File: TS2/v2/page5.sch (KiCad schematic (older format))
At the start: 4 parts, among them U15 HM6264, U16 2764, U17 HM6264, U18 2764

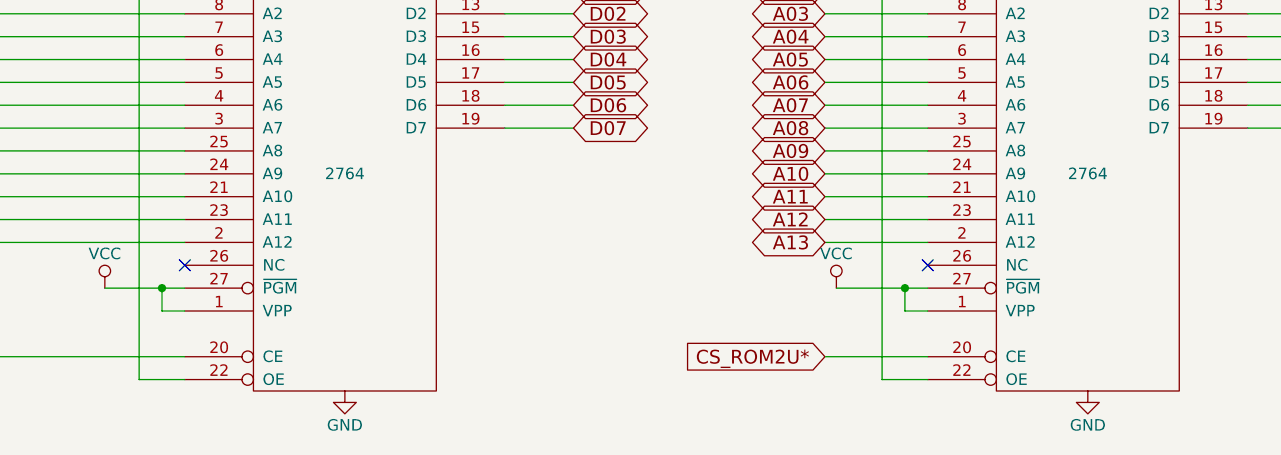
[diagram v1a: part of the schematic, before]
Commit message: Use 28C64 EEPROM instead of 27C64 EPROM.
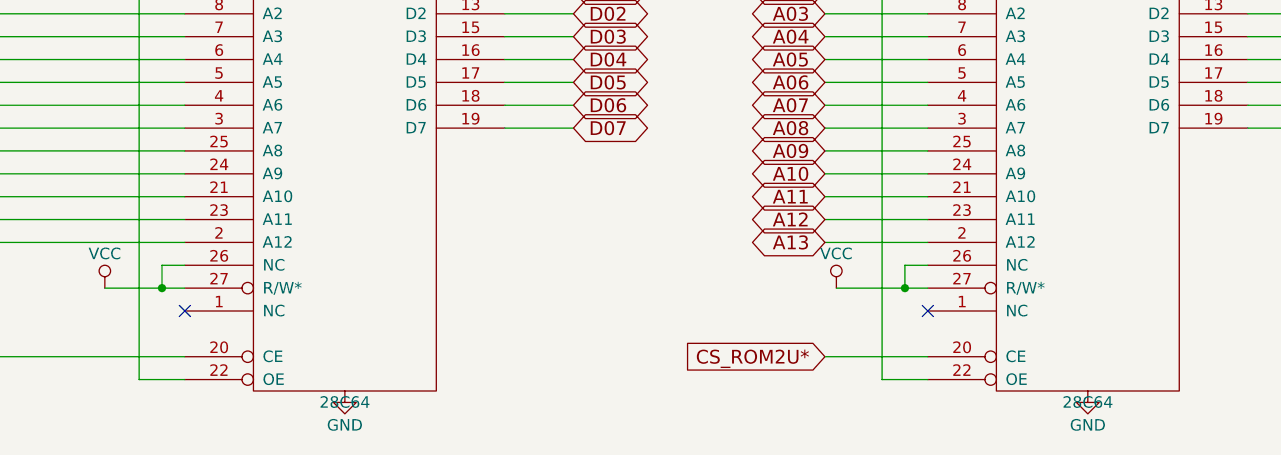
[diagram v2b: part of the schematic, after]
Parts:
- removed U16, U18: 2764, symbol 2764
- added U16, U18: 28C64, symbol 28C64
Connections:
- net A01: now also U16.10 (A0), U18.10 (A0)
- net A02: now also U16.9 (A1), U18.9 (A1)
- net A03: now also U16.8 (A2), U18.8 (A2)
- net A04: now also U16.7 (A3), U18.7 (A3)
- net A05: now also U16.6 (A4), U18.6 (A4)
- net A06: now also U16.5 (A5), U18.5 (A5)
- net A07: now also U16.4 (A6), U18.4 (A6)
- net A08: now also U16.3 (A7), U18.3 (A7)
- net A09: now also U16.25 (A8), U18.25 (A8)
- net A10: now also U16.24 (A9), U18.24 (A9)
- net A11: now also U16.21 (A10), U18.21 (A10)
- net A12: now also U16.23 (A11), U18.23 (A11)
- net A13: now also U16.2 (A12), U18.2 (A12)
- net CS_ROM2L*: now also U16.20 (CE)
- net CS_ROM2U*: now also U18.20 (CE)
- net D00: now also U16.11 (D0)
- net D01: now also U16.12 (D1)
- net D02: now also U16.13 (D2)
- net D03: now also U16.15 (D3)
- net D04: now also U16.16 (D4)
- net D05: now also U16.17 (D5)
- net D06: now also U16.18 (D6)
- net D07: now also U16.19 (D7)
- net D08: now also U18.11 (D0)
- net D09: now also U18.12 (D1)
- net D10: now also U18.13 (D2)
- net D11: now also U18.15 (D3)
- net D12: now also U18.16 (D4)
- net D13: now also U18.17 (D5)
- net D14: now also U18.18 (D6)
- net D15: now also U18.19 (D7)
- net GND: now also U16.14 (GND), U18.14 (GND)
- net R*/W: now also U16.22 (OE), U18.22 (OE)
- net VCC: now also U16.26 (NC), U16.27 (R/W*), U16.28 (VCC), U18.26 (NC), U18.27 (R/W*), U18.28 (VCC)
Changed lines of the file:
@@
 $EndDescr
-$Comp
-L 2764 U16
-U 1 1 57CAE145
-P 4350 5100
-F 0 "U16" H 4100 6100 50  0000 C CNN
-F 1 "2764" H 4350 5100 50  0000 C CNN
-F 2 "" H 4350 5100 50  0000 C CNN
-F 3 "" H 4350 5100 50  0000 C CNN
-	1    4350 5100
-	1    0    0    -1
-$EndComp
-$Comp
-L 2764 U18
-U 1 1 57CAE146
-P 7600 5100
-F 0 "U18" H 7350 6100 50  0000 C CNN
-F 1 "2764" H 7600 5100 50  0000 C CNN
-F 2 "" H 7600 5100 50  0000 C CNN
-F 3 "" H 7600 5100 50  0000 C CNN
-	1    7600 5100
-	1    0    0    -1
-$EndComp
 $Comp
 L HM6264 U15
@@
 Wire Wire Line
 	3300 5600 3650 5600
-Wire Wire Line
-	3650 5700 3550 5700
-Wire Wire Line
-	3550 5700 3550 5600
 $Comp
 L VCC #PWR051
@@
 Wire Wire Line
 	2300 5900 3650 5900
-NoConn ~ 3650 5500
 Wire Wire Line
 	3650 5400 2300 5400
@@
 	1    0    0    -1
 $EndComp
-NoConn ~ 6900 5500
 Text GLabel 6450 4300 0    60   BiDi ~ 0
 A02
@@
 Wire Wire Line
 	6500 5600 6900 5600
-Wire Wire Line
-	6800 5600 6800 5700
-Wire Wire Line
-	6800 5700 6900 5700
 Connection ~ 6800 5600
 $Comp
@@
 Text GLabel 2300 3950 0    60   Input ~ 0
 R*/W
+$Comp
+L 28C64 U16
+U 1 1 57D4FDC8
+P 4350 5100
+F 0 "U16" H 4100 6100 50  0000 C CNN
+F 1 "28C64" H 4350 4100 50  0000 C CNN
+F 2 "" H 4350 5100 50  0000 C CNN
+F 3 "" H 4350 5100 50  0000 C CNN
+	1    4350 5100
+	1    0    0    -1
+$EndComp
+$Comp
+L 28C64 U18
+U 1 1 57D4FDF1
+P 7600 5100
+F 0 "U18" H 7350 6100 50  0000 C CNN
+F 1 "28C64" H 7600 4100 50  0000 C CNN
+F 2 "" H 7600 5100 50  0000 C CNN
+F 3 "" H 7600 5100 50  0000 C CNN
+	1    7600 5100
+	1    0    0    -1
+$EndComp
+Wire Wire Line
+	3550 5500 3650 5500
+Wire Wire Line
+	3550 5500 3550 5600
+NoConn ~ 3650 5700
+Wire Wire Line
+	6900 5500 6800 5500
+Wire Wire Line
+	6800 5500 6800 5600
+NoConn ~ 6900 5700
 $EndSCHEMATC

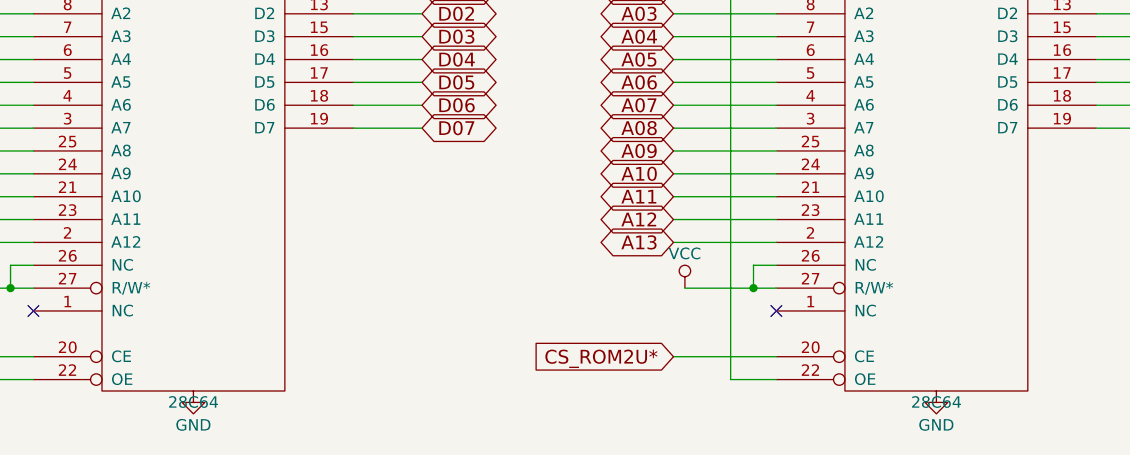
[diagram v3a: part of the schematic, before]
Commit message: Remove two duplicated pullup resistors. Route some signals better.
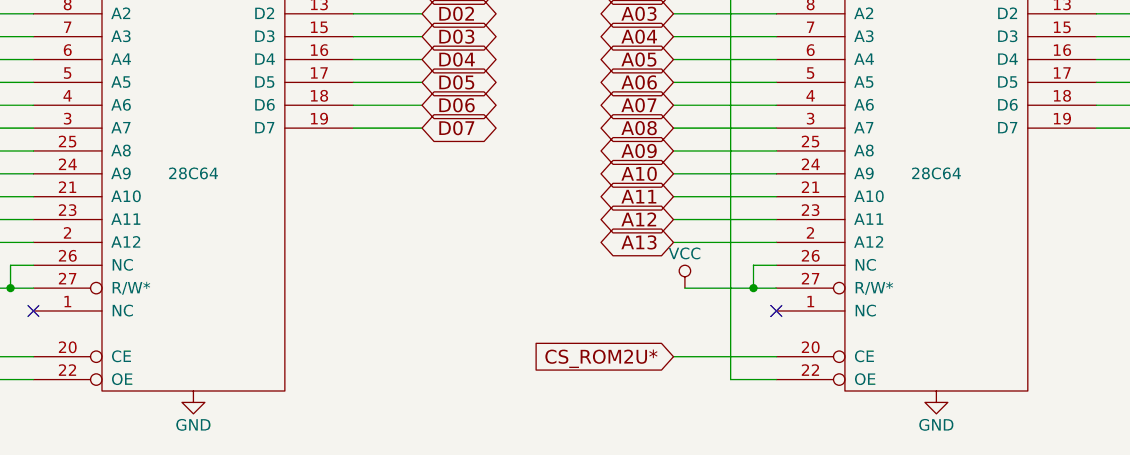
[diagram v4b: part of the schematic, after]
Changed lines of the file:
@@
 Sheet 6 8
 Title "TS2 68000 Single Board Computer"
-Date "2016-09-03"
+Date "2016-11-27"
 Rev "2.0"
 Comp "Jeff Tranter"
@@
 	5050 1650 5350 1650
 $Comp
-L GND #PWR045
+L GND #PWR044
 U 1 1 57C4A627
 P 5050 3250
-F 0 "#PWR045" H 5050 3000 50  0001 C CNN
+F 0 "#PWR044" H 5050 3000 50  0001 C CNN
 F 1 "GND" H 5050 3100 50  0000 C CNN
 F 2 "" H 5050 3250 50  0000 C CNN
@@
 $EndComp
 $Comp
-L VCC #PWR046
+L VCC #PWR045
 U 1 1 57C4A645
 P 5050 3150
-F 0 "#PWR046" H 5050 3000 50  0001 C CNN
+F 0 "#PWR045" H 5050 3000 50  0001 C CNN
 F 1 "VCC" H 5050 3300 50  0000 C CNN
 F 2 "" H 5050 3150 50  0000 C CNN
@@
 $EndComp
 $Comp
-L VCC #PWR047
+L VCC #PWR046
 U 1 1 57C4A66D
 P 8300 3150
-F 0 "#PWR047" H 8300 3000 50  0001 C CNN
+F 0 "#PWR046" H 8300 3000 50  0001 C CNN
 F 1 "VCC" H 8300 3300 50  0000 C CNN
 F 2 "" H 8300 3150 50  0000 C CNN
@@
 $EndComp
 $Comp
-L GND #PWR048
+L GND #PWR047
 U 1 1 57C4A68B
 P 8300 3250
-F 0 "#PWR048" H 8300 3000 50  0001 C CNN
+F 0 "#PWR047" H 8300 3000 50  0001 C CNN
 F 1 "GND" H 8300 3100 50  0000 C CNN
 F 2 "" H 8300 3250 50  0000 C CNN
@@
 A01
 $Comp
-L VCC #PWR049
+L VCC #PWR048
 U 1 1 57C4B0B4
 P 4350 1500
-F 0 "#PWR049" H 4350 1350 50  0001 C CNN
+F 0 "#PWR048" H 4350 1350 50  0001 C CNN
 F 1 "VCC" H 4350 1650 50  0000 C CNN
 F 2 "" H 4350 1500 50  0000 C CNN
@@
 $EndComp
 $Comp
-L GND #PWR050
+L GND #PWR049
 U 1 1 57C4B0FA
 P 4350 3400
-F 0 "#PWR050" H 4350 3150 50  0001 C CNN
+F 0 "#PWR049" H 4350 3150 50  0001 C CNN
 F 1 "GND" H 4350 3250 50  0000 C CNN
 F 2 "" H 4350 3400 50  0000 C CNN
@@
 CS_ROM2L*
 $Comp
-L GND #PWR051
+L GND #PWR050
 U 1 1 57C52013
 P 4350 6050
-F 0 "#PWR051" H 4350 5800 50  0001 C CNN
+F 0 "#PWR050" H 4350 5800 50  0001 C CNN
 F 1 "GND" H 4350 5900 50  0000 C CNN
 F 2 "" H 4350 6050 50  0000 C CNN
@@
 $EndComp
 $Comp
-L VCC #PWR052
+L VCC #PWR051
 U 1 1 57CAE14E
 P 4350 4150
-F 0 "#PWR052" H 4350 4000 50  0001 C CNN
+F 0 "#PWR051" H 4350 4000 50  0001 C CNN
 F 1 "VCC" H 4350 4300 50  0000 C CNN
 F 2 "" H 4350 4150 50  0000 C CNN
@@
 	3300 5600 3650 5600
 $Comp
-L VCC #PWR053
+L VCC #PWR052
 U 1 1 57CAE14F
 P 3300 5600
-F 0 "#PWR053" H 3300 5450 50  0001 C CNN
+F 0 "#PWR052" H 3300 5450 50  0001 C CNN
 F 1 "VCC" H 3300 5750 50  0000 C CNN
 F 2 "" H 3300 5600 50  0000 C CNN
@@
 Connection ~ 3650 3650
 $Comp
-L VCC #PWR054
+L VCC #PWR053
 U 1 1 57CAE150
 P 7600 1500
-F 0 "#PWR054" H 7600 1350 50  0001 C CNN
+F 0 "#PWR053" H 7600 1350 50  0001 C CNN
 F 1 "VCC" H 7600 1650 50  0000 C CNN
 F 2 "" H 7600 1500 50  0000 C CNN
@@
 $EndComp
 $Comp
-L GND #PWR055
+L GND #PWR054
 U 1 1 57CAE151
 P 7600 3400
-F 0 "#PWR055" H 7600 3150 50  0001 C CNN
+F 0 "#PWR054" H 7600 3150 50  0001 C CNN
 F 1 "GND" H 7600 3250 50  0000 C CNN
 F 2 "" H 7600 3400 50  0000 C CNN
@@
 	6450 4200 6900 4200
 $Comp
-L VCC #PWR056
+L VCC #PWR055
 U 1 1 57CAE152
 P 7600 4150
-F 0 "#PWR056" H 7600 4000 50  0001 C CNN
+F 0 "#PWR055" H 7600 4000 50  0001 C CNN
 F 1 "VCC" H 7600 4300 50  0000 C CNN
 F 2 "" H 7600 4150 50  0000 C CNN
@@
 $EndComp
 $Comp
-L GND #PWR057
+L GND #PWR056
 U 1 1 57CAE153
 P 7600 6050
-F 0 "#PWR057" H 7600 5800 50  0001 C CNN
+F 0 "#PWR056" H 7600 5800 50  0001 C CNN
 F 1 "GND" H 7600 5900 50  0000 C CNN
 F 2 "" H 7600 6050 50  0000 C CNN
@@
 Connection ~ 6800 5600
 $Comp
-L VCC #PWR058
+L VCC #PWR057
 U 1 1 57C575E7
 P 6500 5600
-F 0 "#PWR058" H 6500 5450 50  0001 C CNN
+F 0 "#PWR057" H 6500 5450 50  0001 C CNN
 F 1 "VCC" H 6500 5750 50  0000 C CNN
 F 2 "" H 6500 5600 50  0000 C CNN
@@
 P 4350 5100
 F 0 "U16" H 4100 6100 50  0000 C CNN
-F 1 "28C64" H 4350 4100 50  0000 C CNN
+F 1 "28C64" H 4350 5100 50  0000 C CNN
 F 2 "" H 4350 5100 50  0000 C CNN
 F 3 "" H 4350 5100 50  0000 C CNN
@@
 P 7600 5100
 F 0 "U18" H 7350 6100 50  0000 C CNN
-F 1 "28C64" H 7600 4100 50  0000 C CNN
+F 1 "28C64" H 7600 5100 50  0000 C CNN
 F 2 "" H 7600 5100 50  0000 C CNN
 F 3 "" H 7600 5100 50  0000 C CNN

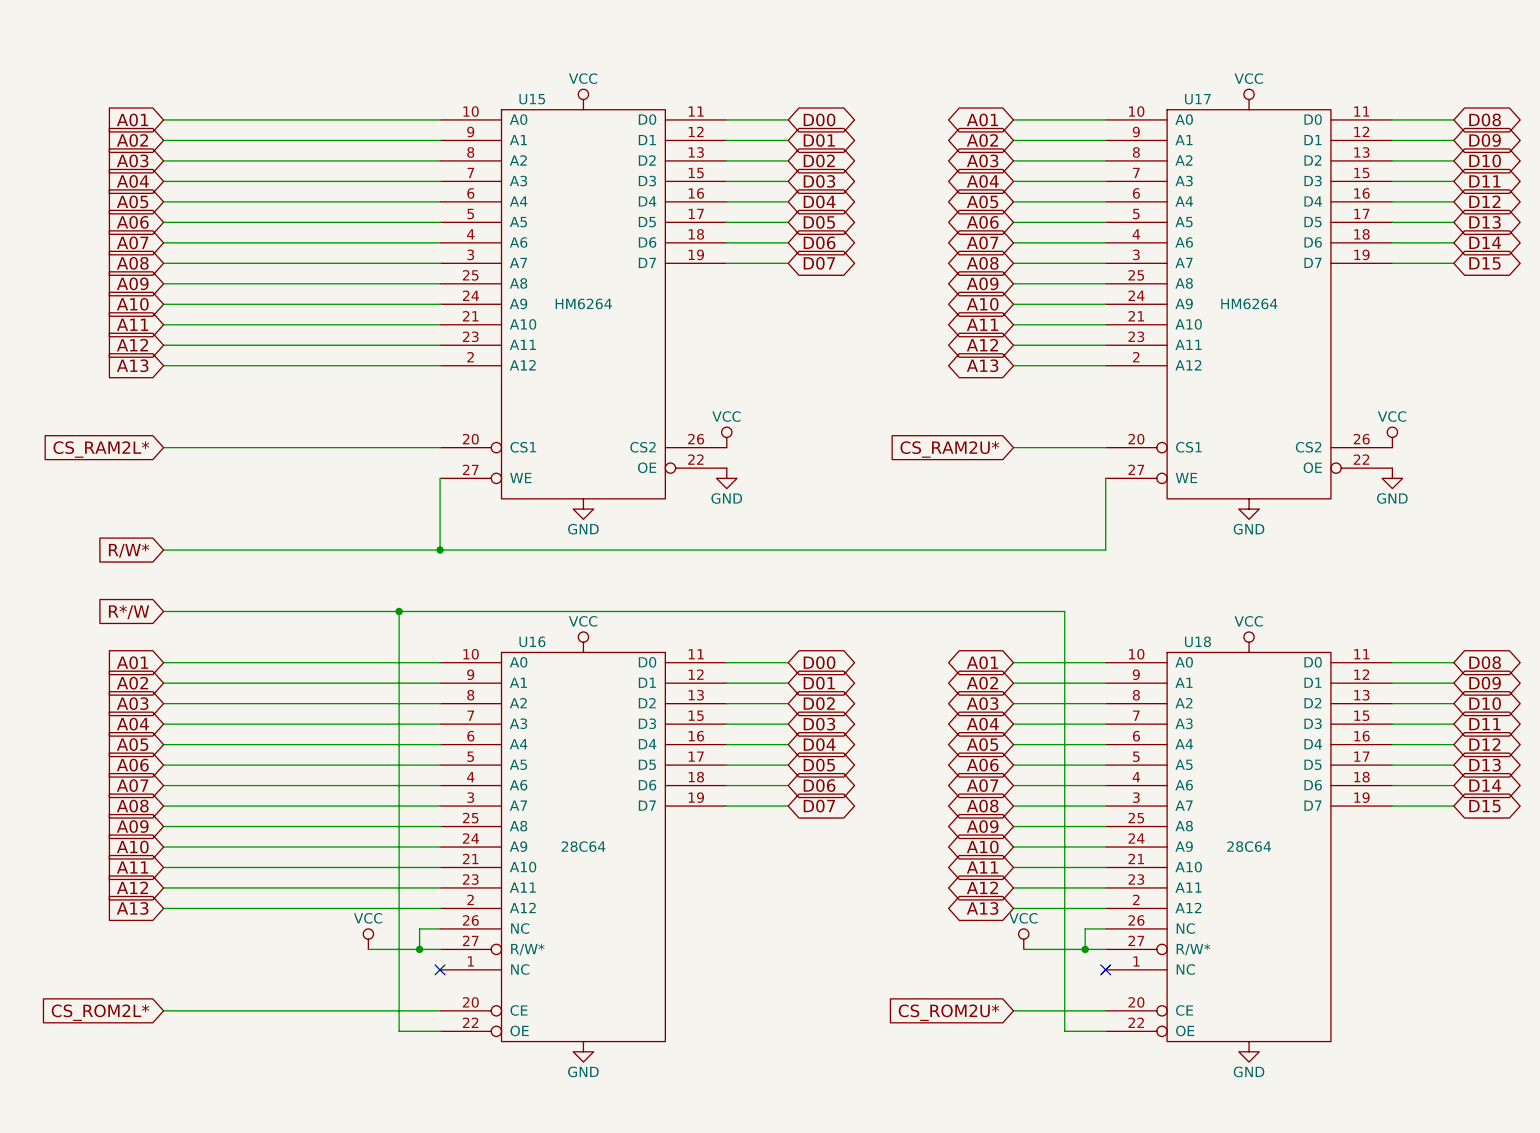
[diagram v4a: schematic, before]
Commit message: Label RAM and ROM chips with address ranges.
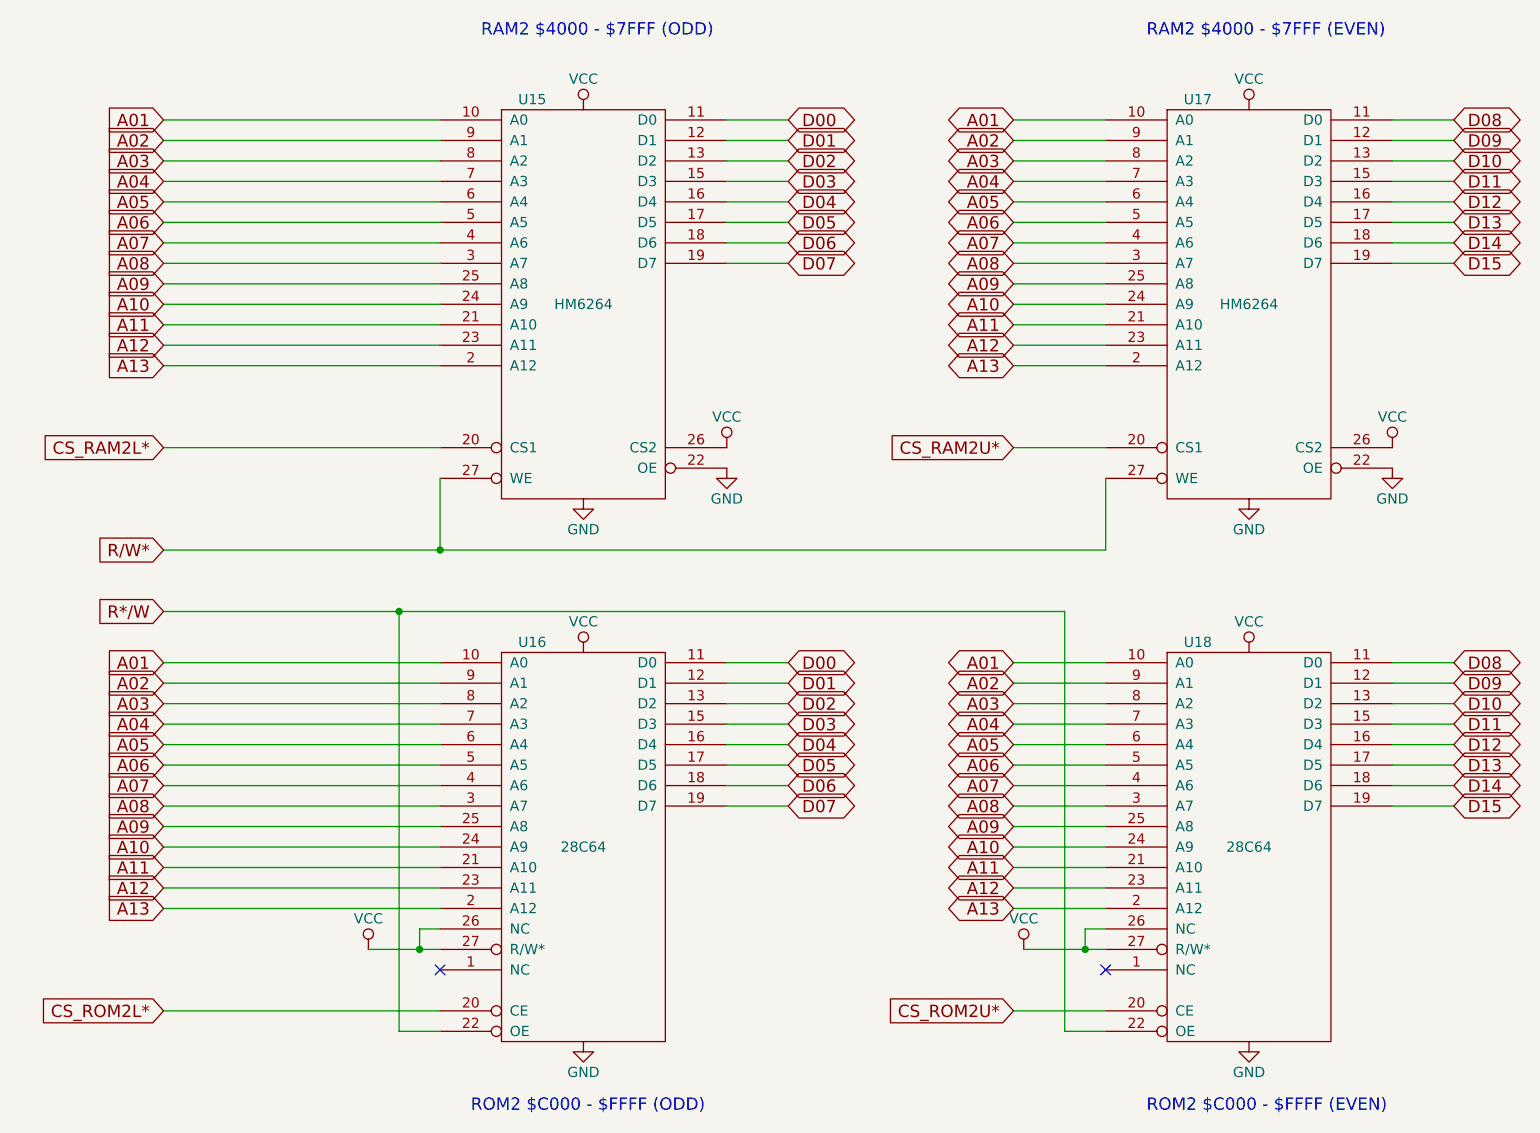
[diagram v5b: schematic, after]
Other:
- note added: "RAM2 $4000 - $7FFF (EVEN)"
- note added: "RAM2 $4000 - $7FFF (ODD)"
- note added: "ROM2 $C000 - $FFFF (EVEN)"
- note added: "ROM2 $C000 - $FFFF (ODD)"
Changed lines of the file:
@@
 	6800 5500 6800 5600
 NoConn ~ 6900 5700
+Text Notes 3850 1150 0    60   ~ 0
+RAM2 $4000 - $7FFF (ODD)
+Text Notes 7100 1150 0    60   ~ 0
+RAM2 $4000 - $7FFF (EVEN)
+Text Notes 3800 6400 0    60   ~ 0
+ROM2 $C000 - $FFFF (ODD)
+Text Notes 7100 6400 0    60   ~ 0
+ROM2 $C000 - $FFFF (EVEN)
 $EndSCHEMATC
